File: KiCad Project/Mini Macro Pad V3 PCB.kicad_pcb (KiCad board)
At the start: 4 copper layers, 65 x 65 mm, 97 parts, among them J1 USB_C_Receptacle_USB2.0_14P, SW1 SW_Push bootsel, SW10 SW_Push, SW11 SW_Push, SW12 SW_Push, SW13 SW_Push, SW14 SW_Push, SW15 SW_Push, SW16 SW_Push, SW17 SW_Push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

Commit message: small tweaks before ordering
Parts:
- added TP10: ~, TestPoint:TestPoint_Pad_1.5x1.5mm, B.Cu at (113.2, 115.5)
- added TP9: ~, TestPoint:TestPoint_Pad_1.5x1.5mm, B.Cu at (113.2, 108.4)
- C14, C15, C16, C17, C18, C19, C20, C21, C22, C23: value 104 -> 100pf
- R3, R4: value 27.4 -> 27
- SW1, SW10, SW11, SW12, SW13, SW14, SW15, SW16, SW17, SW18, SW19, SW2, SW20, SW21, SW3, SW4, SW5, SW6, SW7, SW8, SW9: footprint Button_Switch_THT:SW_PUSH_6mm_H4.3mm -> Button_Switch_THT:SW_PUSH_6mm_H5mm
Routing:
- net /NEOPIXEL_DIN: track 37.6 -> 43.0 mm

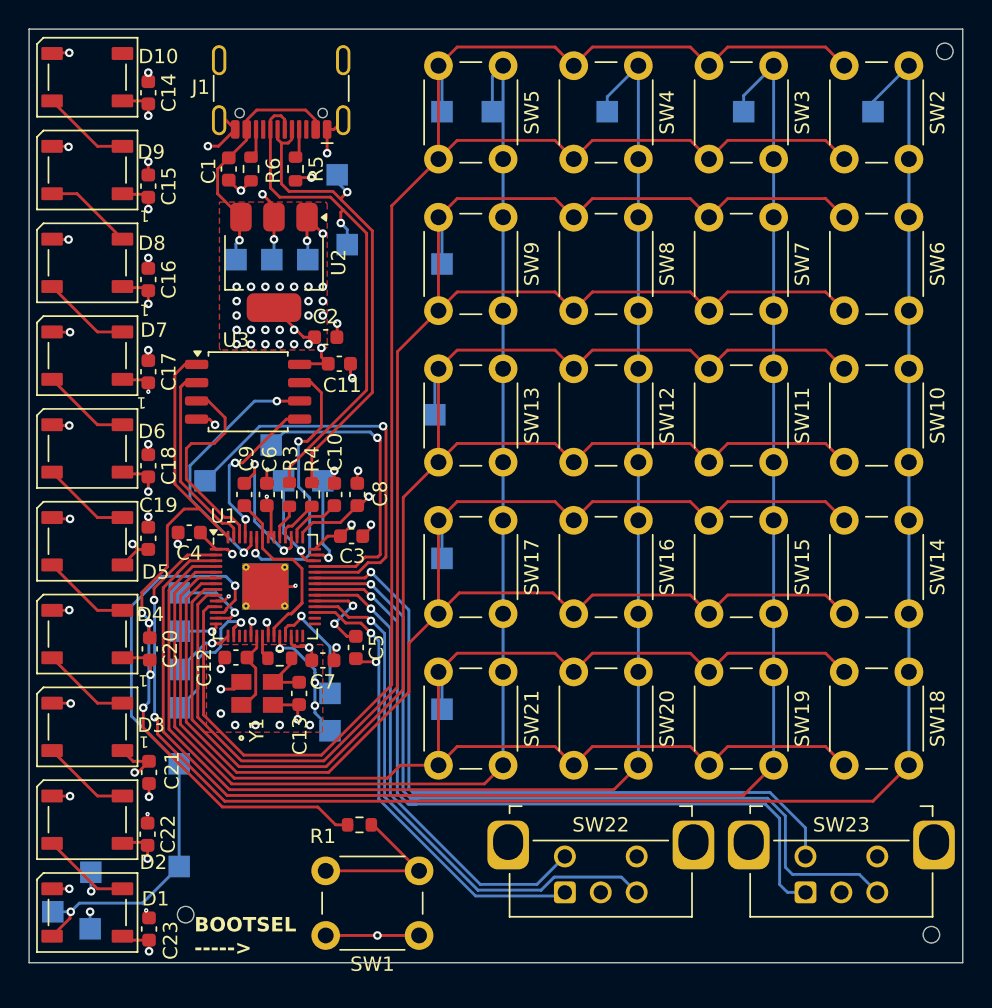
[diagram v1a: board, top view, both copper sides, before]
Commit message: Changed USB C footprint
changed because of part availability.
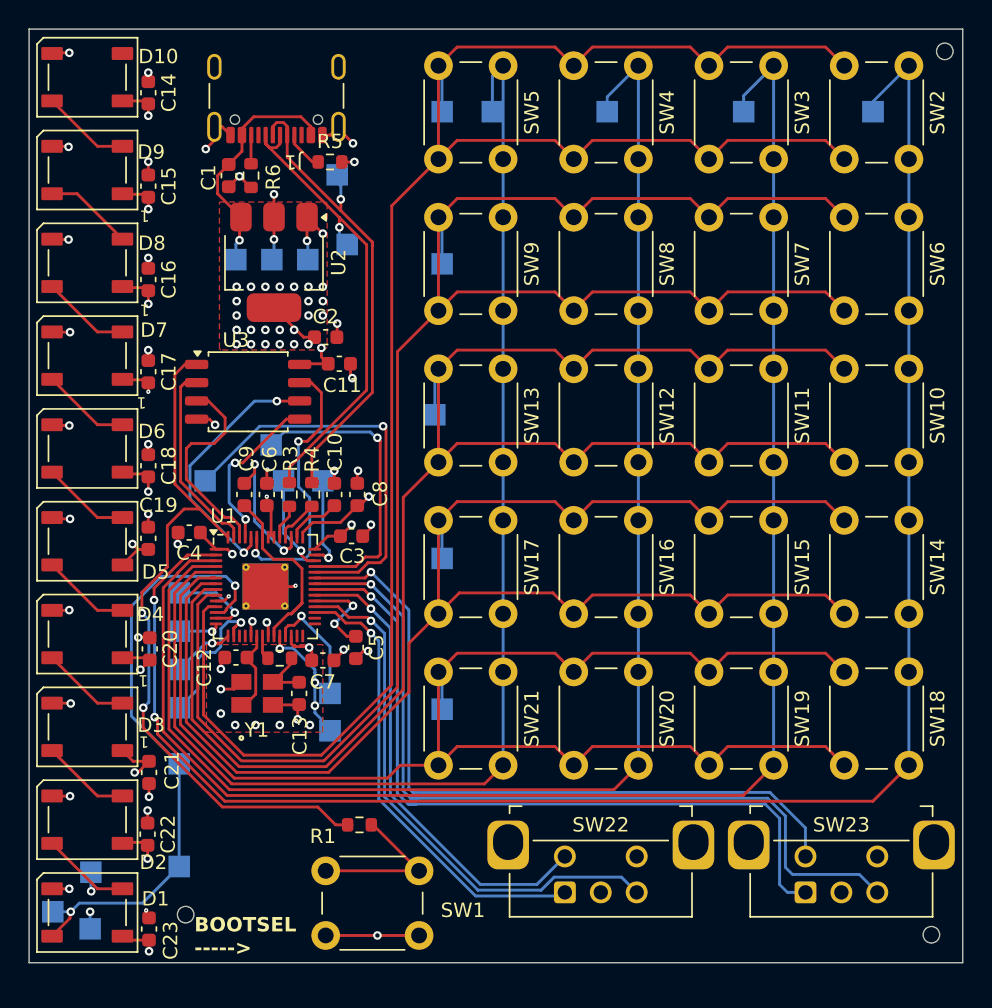
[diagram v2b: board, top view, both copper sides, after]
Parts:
- J1: footprint Connector_USB:USB_C_Receptacle_HCTL_HC-TYPE-C-16P-01A -> Connector_USB:USB_C_Receptacle_GCT_USB4105-xx-A_16P_TopMnt_Horizontal
- moved R5 2.45 mm to (123.7, 66.5), turned to 0 degrees
- moved J1 0.57 mm to (120.0, 61.0)
- moved C1 0.46 mm to (116.7, 67.5)
- moved R6 0.46 mm to (118.2, 67.5)
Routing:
- net /USB_D+: track 36.2 -> 33.3 mm
- net Net-(J1-CC1): track 1.91 -> 2.79 mm
- net GND: track 60.8 -> 60.1 mm
- net VBUS: track 16.0 -> 16.5 mm

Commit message: final save before first prototype order
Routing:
- net GND: track 60.1 -> 58.8 mm
- net /USB_D+: track 33.3 -> 32.5 mm
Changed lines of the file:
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@@
 			(remove_unused_layers yes)
 			(keep_end_layers yes)
-			(zone_layer_connections)
+			(zone_layer_connections "In1.Cu")
 			(net 1 "GND")
 			(pinfunction "GND")
@@
 			(remove_unused_layers yes)
 			(keep_end_layers yes)
-			(zone_layer_connections)
+			(zone_layer_connections "In1.Cu")
 			(net 1 "GND")
 			(pinfunction "GND")
@@
 			(remove_unused_layers yes)
 			(keep_end_layers yes)
-			(zone_layer_connections)
+			(zone_layer_connections "In1.Cu")
 			(net 1 "GND")
 			(pinfunction "GND")
@@
 			(remove_unused_layers yes)
 			(keep_end_layers yes)
-			(zone_layer_connections)
+			(zone_layer_connections "In1.Cu")
 			(net 1 "GND")
 			(pinfunction "GND")
@@
 		(tags "resistor")
 		(property "Reference" "R5"
-			(at 0 -1.43 0)
+			(at 0 1.4 0)
 			(layer "F.SilkS")
 			(effects
@@
 			(remove_unused_layers yes)
 			(keep_end_layers yes)
-			(zone_layer_connections)
+			(zone_layer_connections "In1.Cu")
 			(net 1 "GND")
 			(pinfunction "C")
@@
 			(remove_unused_layers yes)
 			(keep_end_layers yes)
-			(zone_layer_connections)
+			(zone_layer_connections "In1.Cu")
 			(net 1 "GND")
 			(pinfunction "S2")
@@
 			(remove_unused_layers yes)
 			(keep_end_layers yes)
-			(zone_layer_connections)
+			(zone_layer_connections "In1.Cu")
 			(net 1 "GND")
 			(pinfunction "C")
@@
 			(remove_unused_layers yes)
 			(keep_end_layers yes)
-			(zone_layer_connections)
+			(zone_layer_connections "In1.Cu")
 			(net 1 "GND")
 			(pinfunction "S2")
@@
 	)
 	(segment
-		(start 115.65 65)
-		(end 115.65 64.055)
-		(width 0.2)
-		(layer "F.Cu")
-		(net 1)
-	)
-	(segment
 		(start 126.55 91.975)
 		(end 125.975 92.55)
@@
 	)
 	(segment
-		(start 118.2 68.275)
-		(end 118.175 68.275)
-		(width 0.2)
-		(layer "F.Cu")
-		(net 1)
-	)
-	(segment
 		(start 123.715 64.63)
 		(end 124.29 64.055)
@@
 	)
 	(segment
-		(start 125.725 101.175)
-		(end 125.725 101.3)
-		(width 0.2)
-		(layer "F.Cu")
-		(net 1)
-	)
-	(segment
 		(start 123.17 64.63)
 		(end 123.715 64.63)
@@
 	)
 	(segment
-		(start 111 112.525)
-		(end 111 112.3)
-		(width 0.2)
-		(layer "F.Cu")
-		(net 1)
-	)
-	(segment
 		(start 117.026999 103.2)
 		(end 117.527 102.699999)
@@
 	)
 	(segment
+		(start 111.1 119.125)
+		(end 111.1 118.6)
+		(width 0.2)
+		(layer "F.Cu")
+		(net 1)
+	)
+	(segment
 		(start 125.4 66.5)
 		(end 124.525 66.5)
@@
 	)
 	(segment
-		(start 124.29 64.055)
-		(end 124.29 64.19)
-		(width 0.2)
-		(layer "F.Cu")
-		(net 1)
-	)
-	(segment
 		(start 125.25 81.55)
 		(end 125.125 81.425)
@@
 	)
 	(segment
+		(start 111.1 118.6)
+		(end 111.35 118.35)
+		(width 0.2)
+		(layer "F.Cu")
+		(net 1)
+	)
+	(segment
 		(start 118.2 99.5)
 		(end 118.2 98.575311)
@@
 	)
 	(segment
-		(start 110.9 119.3325)
-		(end 110.9 118.6)
-		(width 0.2)
-		(layer "F.Cu")
-		(net 1)
-	)
-	(segment
 		(start 111.05 74.115)
 		(end 111.05 73.1825)
@@
 	)
 	(segment
-		(start 123.975 101.2)
-		(end 123.975 101.125)
+		(start 111 112.3)
+		(end 111 111.65)
 		(width 0.2)
 		(layer "F.Cu")
@@
 	)
 	(segment
-		(start 111 112.3)
-		(end 111 111.65)
+		(start 105.55 117.1)
+		(end 104.35 117.1)
 		(width 0.2)
 		(layer "F.Cu")
@@
 	)
 	(segment
-		(start 105.55 117.1)
-		(end 104.35 117.1)
+		(start 127 120.35)
+		(end 127 120.25)
 		(width 0.2)
 		(layer "F.Cu")
@@
 	)
 	(via micro
+		(at 111.35 118.35)
+		(size 0.6)
+		(drill 0.3)
+		(layers "F.Cu" "In1.Cu")
+		(net 1)
+	)
+	(via micro
 		(at 126.35 100.55)
 		(size 0.6)
@@
 	)
 	(via micro
-		(at 110.9 118.6)
-		(size 0.3)
-		(drill 0.1)
-		(layers "F.Cu" "In1.Cu")
-		(net 1)
-	)
-	(via micro
 		(at 111.05 91)
 		(size 0.6)
@@
 	)
 	(segment
-		(start 117.57 64.171176)
-		(end 117.57 64.63)
-		(width 0.2)
-		(layer "F.Cu")
-		(net 2)
-	)
-	(segment
 		(start 122.37 64.055001)
 		(end 121.667999 63.353)
@@
 	)
 	(segment
-		(start 111.125 101.225)
-		(end 111.2 101.225)
+		(start 119.4 92.625)
+		(end 119.6 92.425)
 		(width 0.2)
 		(layer "F.Cu")
@@
 	)
 	(segment
-		(start 119.4 92.625)
-		(end 119.6 92.425)
+		(start 119.327175 89.825)
+		(end 119.327175 90.398325)
 		(width 0.2)
 		(layer "F.Cu")
@@
 	)
 	(segment
+		(start 119.327175 90.398325)
+		(end 119.3005 90.425)
+		(width 0.2)
+		(layer "F.Cu")
+		(net 3)
+	)
+	(segment
 		(start 114.675 92.375)
 		(end 115.7625 93.4625)
@@
 	)
 	(segment
-		(start 119.3005 89.8005)
-		(end 119.3005 90.425)
-		(width 0.2)
-		(layer "F.Cu")
-		(net 3)
-	)
-	(segment
 		(start 111.1 120.675)
 		(end 111.1 121.45)
@@
 	)
 	(segment
-		(start 111 113.8675)
-		(end 109.321389 113.8675)
+		(start 111.05 81.875)
+		(end 111.05 82.75)
 		(width 0.2)
 		(layer "F.Cu")
@@
 	)
 	(segment
-		(start 119.3 89.8)
-		(end 119.3005 89.8005)
+		(start 111 113.8675)
+		(end 109.321389 113.8675)
 		(width 0.2)
 		(layer "F.Cu")
@@
 	)
 	(segment
-		(start 111.05 81.6675)
-		(end 111.05 82.5)
-		(width 0.2)
-		(layer "F.Cu")
-		(net 3)
-	)
-	(segment
 		(start 122.2 79.125)
 		(end 122.625 78.7)
@@
 		(net 3)
 	)
-	(via micro
-		(at 111.05 82.5)
-		(size 0.3)
-		(drill 0.1)
-		(layers "F.Cu" "In2.Cu")
+	(via
+		(at 111.05 82.75)
+		(size 0.6)
+		(drill 0.3)
+		(layers "F.Cu" "B.Cu")
 		(net 3)
 	)
@@
 	)
 	(via micro
-		(at 119.3 89.8)
-		(size 0.3)
-		(drill 0.1)
-		(layers "F.Cu" "In2.Cu")
-		(net 3)
-	)
-	(via micro
 		(at 111 115)
 		(size 0.6)
@@
 		(net 3)
 	)
+	(via micro
+		(at 119.327175 89.825)
+		(size 0.6)
+		(drill 0.3)
+		(layers "F.Cu" "In2.Cu")
+		(net 3)
+	)
 	(segment
 		(start 124.003226 98.651756)
@@
 	)
 	(segment
-		(start 118.2 64.65)
-		(end 118.22 64.63)
-		(width 0.2)
-		(layer "F.Cu")
-		(net 18)
-	)
-	(segment
 		(start 121.22 65.245)
 		(end 121.22 64.63)
@@
 	)
 	(segment
-		(start 126.575 112.65)
-		(end 126.7 112.65)
-		(width 0.2)
-		(layer "F.Cu")
-		(net 20)
-	)
-	(segment
 		(start 123.4 115.85)
 		(end 129.9 115.85)
@@
 	)
 	(segment
-		(start 124.35 71.7)
-		(end 124.9 72.25)
-		(width 0.2)
-		(layer "B.Cu")
-		(net 22)
-	)
-	(segment
 		(start 126.65 82.5513)
 		(end 122.4335 86.7678)
 		(width 0.2)
 		(layer "F.Cu")
-		(net 23)
-	)
-	(segment
-		(start 126.65 72.0839)
-		(end 126.65 72.3)
-		(width 0.2)
-		(layer "F.Cu")

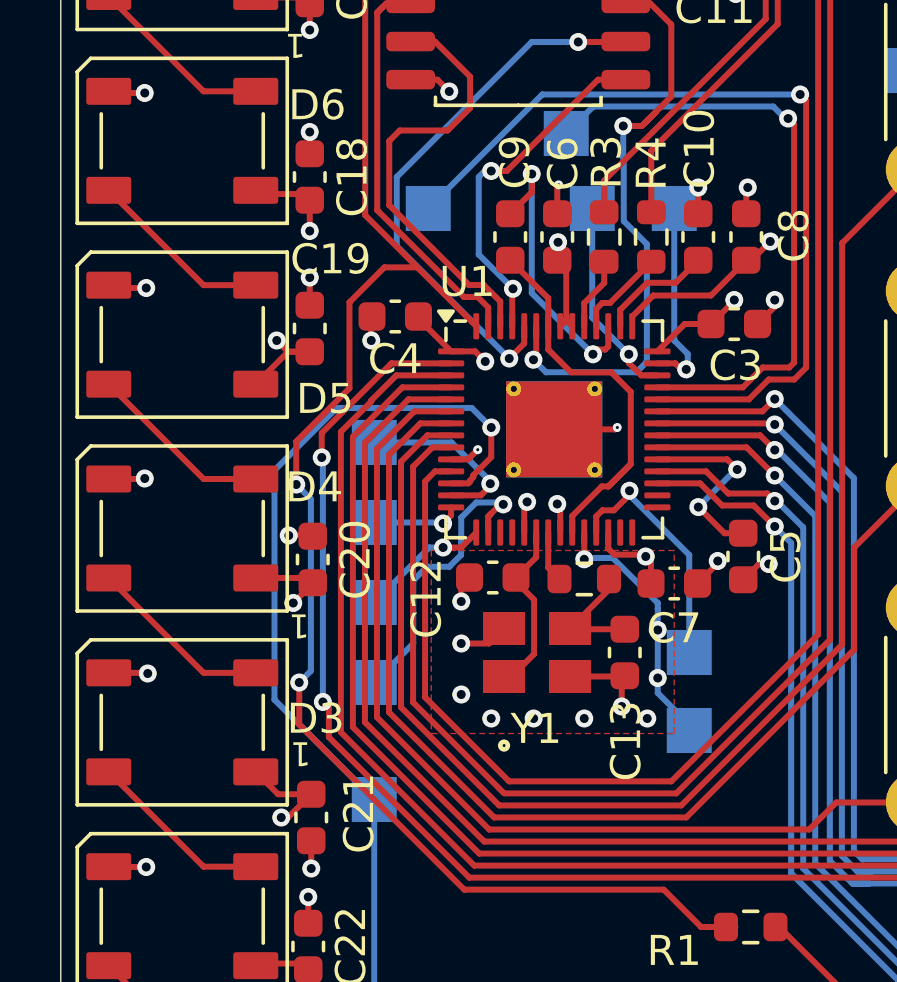
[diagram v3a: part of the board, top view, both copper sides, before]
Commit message: removed holes smaller than .2mm
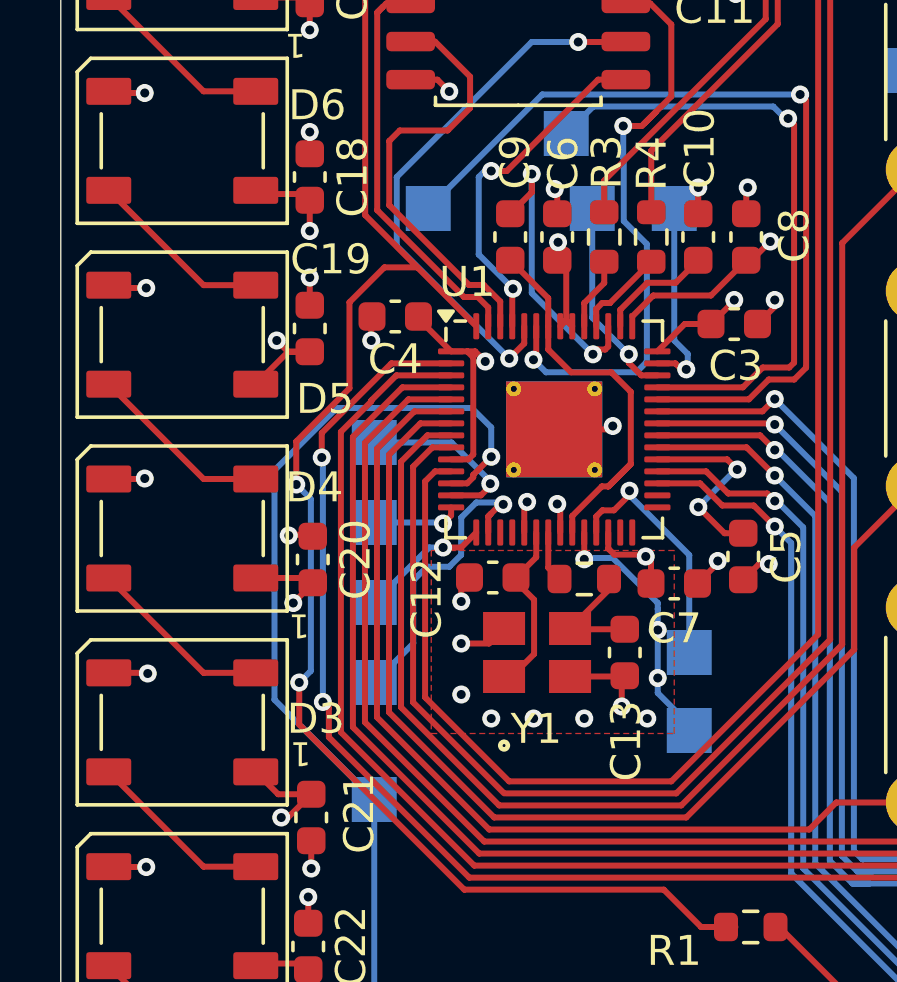
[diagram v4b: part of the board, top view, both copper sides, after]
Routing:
- net +3.3V: track 67.6 -> 70.9 mm, vias 48 -> 47
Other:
- board text added: "WayWayWay"
- board text removed: "JLCJLCJLCJLC"
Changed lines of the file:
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@@
 		)
 	)
-	(gr_text "JLCJLCJLCJLC"
+	(gr_text "WayWayWay"
 		(at 164.6 121.65 0)
 		(layer "B.SilkS")
@@
 	)
 	(segment
+		(start 119.3005 88.875)
+		(end 119.3005 88.133835)
+		(width 0.2)
+		(layer "F.Cu")
+		(net 1)
+	)
+	(segment
 		(start 111.05 91.925)
 		(end 111.05 91)
@@
 	)
 	(segment
+		(start 119.3005 88.133835)
+		(end 119.216665 88.05)
+		(width 0.2)
+		(layer "F.Cu")
+		(net 1)
+	)
+	(segment
 		(start 123.17 64.63)
 		(end 123.715 64.63)
@@
 	)
 	(segment
-		(start 119.3005 87.957117)
-		(end 119.3457 87.911917)
-		(width 0.2)
-		(layer "F.Cu")
-		(net 1)
-	)
-	(segment
 		(start 105.461111 65.411111)
 		(end 105.5 65.45)
@@
 	)
 	(segment
+		(start 119.2 96.0625)
+		(end 121.0385 96.0625)
+		(width 0.2)
+		(layer "F.Cu")
+		(net 1)
+	)
+	(segment
 		(start 115.05 65.6)
 		(end 115.65 65)
@@
 	)
 	(segment
-		(start 121.2375 96.0625)
-		(end 121.3 96)
-		(width 0.2)
-		(layer "F.Cu")
-		(net 1)
-	)
-	(segment
 		(start 111.05 67.615)
 		(end 111.05 66.4825)
@@
 	)
 	(segment
-		(start 119.2 96.0625)
-		(end 121.2375 96.0625)
-		(width 0.2)
-		(layer "F.Cu")
-		(net 1)
-	)
-	(segment
 		(start 111.05 87.0825)
 		(end 111.05 86.15)
@@
 	)
 	(segment
-		(start 119.3005 88.875)
-		(end 119.3005 87.957117)
-		(width 0.2)
-		(layer "F.Cu")
-		(net 1)
-	)
-	(segment
 		(start 125.125 81.425)
 		(end 125.125 80.55)
@@
 	)
 	(segment
+		(start 121.0385 96.0625)
+		(end 121.151 95.95)
+		(width 0.2)
+		(layer "F.Cu")
+		(net 1)
+	)
+	(segment
 		(start 121.45 105.3)
 		(end 121.3 105.45)
@@
 	)
 	(via micro
-		(at 119.3457 87.911917)
-		(size 0.3)
-		(drill 0.1)
-		(layers "F.Cu" "In1.Cu")
-		(net 1)
-	)
-	(via micro
 		(at 125.65 88)
 		(size 0.6)
@@
 		(size 0.6)
 		(drill 0.3)
-		(layers "F.Cu" "In1.Cu")
-		(net 1)
-	)
-	(via micro
-		(at 121.3 96)
-		(size 0.3)
-		(drill 0.1)
 		(layers "F.Cu" "In1.Cu")
 		(net 1)
@@
 	)
 	(via micro
+		(at 121.151 95.95)
+		(size 0.6)
+		(drill 0.3)
+		(layers "F.Cu" "In1.Cu")
+		(net 1)
+	)
+	(via micro
 		(at 105.6 110.65)
 		(size 0.6)
@@
 	(via micro
 		(at 117.099997 105.7)
+		(size 0.6)
+		(drill 0.3)
+		(layers "F.Cu" "In1.Cu")
+		(net 1)
+	)
+	(via micro
+		(at 119.216665 88.05)
 		(size 0.6)
 		(drill 0.3)
@@
 	)
 	(segment
-		(start 115.7625 97.0625)
-		(end 116.326463 97.0625)
-		(width 0.2)
-		(layer "F.Cu")
-		(net 3)
-	)
-	(segment
 		(start 122.1885 100.2385)
 		(end 121.203226 100.2385)
@@
 	)
 	(segment
-		(start 116.326463 97.0625)
-		(end 116.649998 96.738965)
+		(start 116.3375 97.0625)
+		(end 115.7625 97.0625)
 		(width 0.2)
 		(layer "F.Cu")
@@
 	)
 	(segment
+		(start 116.501 93.6635)
+		(end 116.3 93.4625)
+		(width 0.2)
+		(layer "F.Cu")
+		(net 3)
+	)
+	(segment
 		(start 115.7625 93.4625)
-		(end 116.5625 93.4625)
+		(end 116.3 93.4625)
 		(width 0.2)
 		(layer "F.Cu")
@@
 	)
 	(segment
+		(start 116.3 93.4625)
+		(end 116.5625 93.4625)
+		(width 0.2)
+		(layer "F.Cu")
+		(net 3)
+	)
+	(segment
 		(start 124.425 92.55)
 		(end 123.55 92.55)
@@
 	)
 	(segment
+		(start 116.501 96.899)
+		(end 116.3375 97.0625)
+		(width 0.2)
+		(layer "F.Cu")
+		(net 3)
+	)
+	(segment
 		(start 114.675 92.375)
 		(end 115.7625 93.4625)
@@
 		(start 111.05 62.25)
 		(end 109.25 62.25)
+		(width 0.2)
+		(layer "F.Cu")
+		(net 3)
+	)
+	(segment
+		(start 116.501 96.899)
+		(end 116.501 93.6635)
 		(width 0.2)
 		(layer "F.Cu")
@@
 		(keep_end_layers yes)
 		(zone_layer_connections)
-		(net 3)
-	)
-	(via micro
-		(at 116.649998 96.738965)
-		(size 0.3)
-		(drill 0.1)
-		(layers "F.Cu" "In2.Cu")
 		(net 3)
 	)
@@
 	)
 	(segment
+		(start 117.100001 96.976833)
+		(end 116.501 97.575834)
+		(width 0.2)
+		(layer "F.Cu")
+		(net 10)
+	)
+	(segment
 		(start 105.6 119.15)
 		(end 104.35 120.4)
@@
 	)
 	(segment
-		(start 117.099998 96.991226)
-		(end 117.099998 96)
+		(start 116.501 97.575834)
+		(end 116.501 97.659274)
 		(width 0.2)
 		(layer "F.Cu")
@@
 	)
 	(segment
-		(start 116.4 97.760274)
-		(end 116.501 97.659274)
+		(start 117.100001 96.976833)
+		(end 117.099998 96.976836)
 		(width 0.2)
 		(layer "F.Cu")
@@
 	)
 	(segment
-		(start 116.3375 97.8625)
-		(end 116.4 97.8)
+		(start 116.297774 97.8625)
+		(end 115.7625 97.8625)
+		(width 0.2)
+		(layer "F.Cu")
+		(net 10)
+	)
+	(segment
+		(start 116.501 97.659274)
+		(end 116.297774 97.8625)
 		(width 0.2)
 		(layer "F.Cu")
@@
 	)
 	(segment
-		(start 116.4 97.8)
-		(end 116.4 97.760274)
+		(start 117.099998 96.976836)
+		(end 117.099998 96.991226)
 		(width 0.2)
 		(layer "F.Cu")
 		(net 10)
 	)
-	(segment
-		(start 116.501 97.590224)
-		(end 117.099998 96.991226)
-		(width 0.2)
-		(layer "F.Cu")
-		(net 10)
-	)
-	(segment
-		(start 116.501 97.659274)
-		(end 116.501 97.590224)
-		(width 0.2)
-		(layer "F.Cu")
-		(net 10)
-	)
-	(segment
-		(start 115.7625 97.8625)
-		(end 116.3375 97.8625)
-		(width 0.2)
-		(layer "F.Cu")
-		(net 10)
-	)
 	(via
-		(at 117.099998 96)
+		(at 117.100001 96.976833)
 		(size 0.6)
 		(drill 0.3)
@@
 	)
 	(segment
-		(start 116.449998 95.35)
-		(end 117.099998 96)
+		(start 117.100001 96.976833)
+		(end 117.099998 96.97683)
 		(width 0.2)
 		(layer "B.Cu")
@@
 	(segment
 		(start 109.875 105.075)
+		(end 113.2 108.4)
+		(width 0.2)
+		(layer "B.Cu")
+		(net 10)
+	)
+	(segment
+		(start 109.875 97.425)
+		(end 109.875 105.075)
+		(width 0.2)
+		(layer "B.Cu")
+		(net 10)
+	)
+	(segment
+		(start 117.099998 96)
+		(end 116.449998 95.35)
+		(width 0.2)
+		(layer "B.Cu")
+		(net 10)
+	)
+	(segment
+		(start 111.95 95.35)
 		(end 109.875 97.425)
 		(width 0.2)
@@
 	)
 	(segment
-		(start 109.875 97.425)
-		(end 111.95 95.35)
-		(width 0.2)
-		(layer "B.Cu")
-		(net 10)
-	)
-	(segment
-		(start 113.2 108.4)
-		(end 109.875 105.075)
-		(width 0.2)
-		(layer "B.Cu")
-		(net 10)
-	)
-	(segment
 		(start 105.65 118.7)
 		(end 106.251 118.099)
@@
 	)
 	(segment
-		(start 111.95 95.35)
-		(end 116.449998 95.35)
+		(start 116.449998 95.35)
+		(end 111.95 95.35)
 		(width 0.2)
 		(layer "B.Cu")
@@
 		(width 0.2)
 		(layer "B.Cu")
+		(net 10)
+	)
+	(segment
+		(start 117.099998 96.97683)
+		(end 117.099998 96)
+		(width 0.2)
+		(layer "B.Cu")
